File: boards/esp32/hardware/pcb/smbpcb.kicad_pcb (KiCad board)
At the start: 2 copper layers, 85.4 x 70.4 mm, 70 parts, among them IC1 MiCS-6814, J1 USB_B_Micro, J2 PMS7003, Q1 SUD08P06-155L, SW1 RESET, SW2 RESET, U1 MCP73831-2-OT, U2 SGM6603-5.0YN6G_TR, U3 ESP32-WROOM-32, U4 SSD1306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

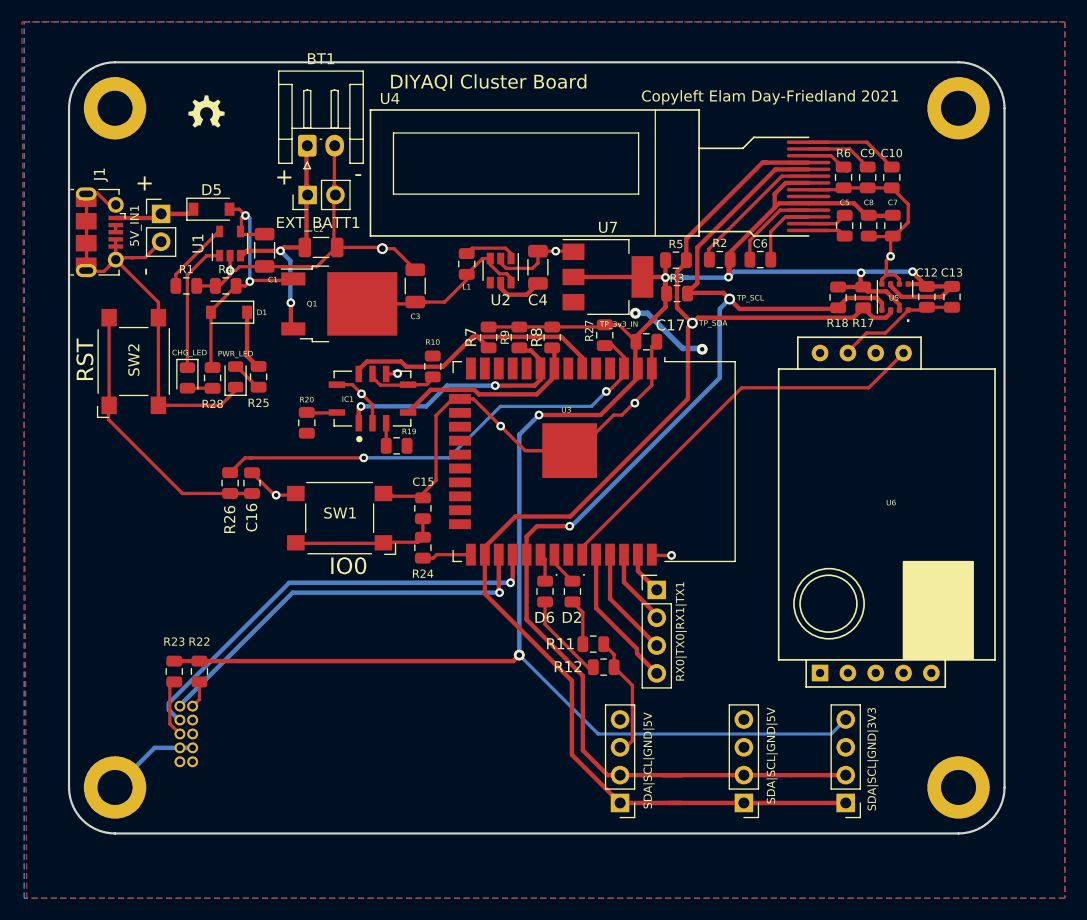
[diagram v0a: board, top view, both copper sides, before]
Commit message: went through DRC
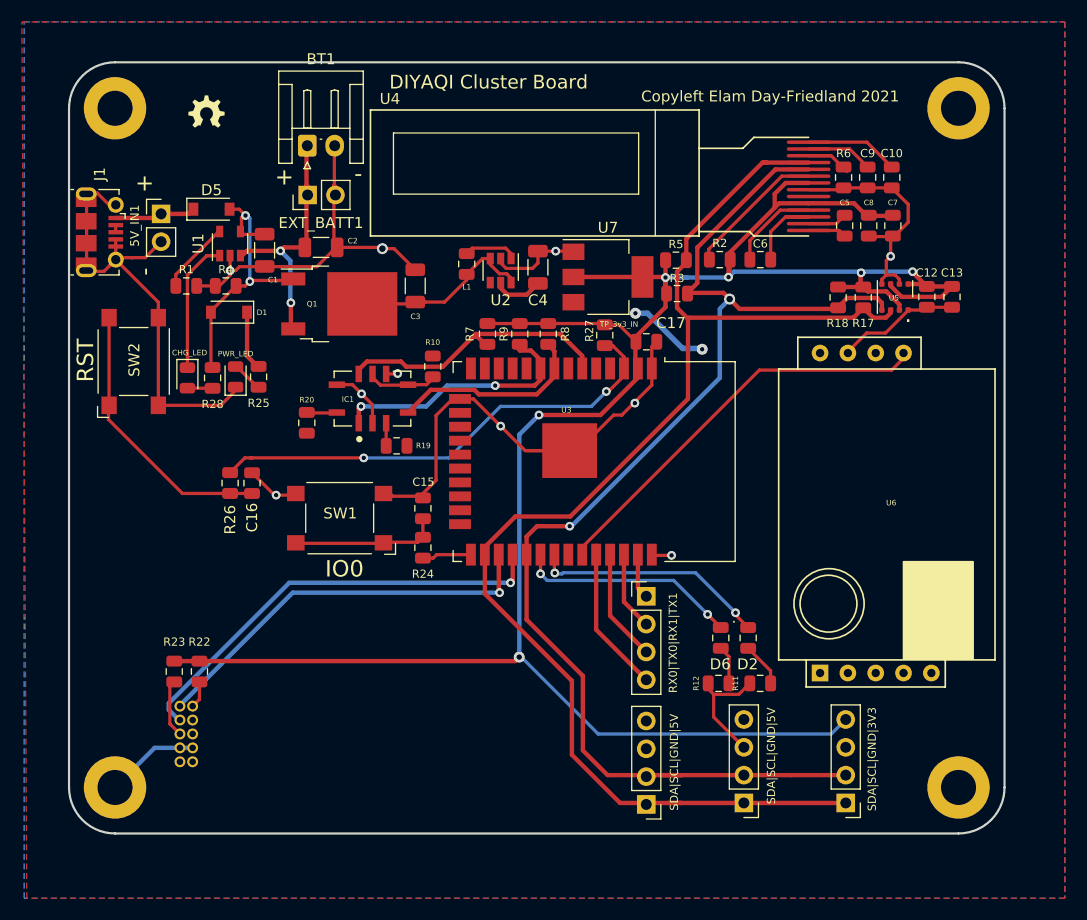
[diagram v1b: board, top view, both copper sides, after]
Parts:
- moved D2 16.6 mm to (113.5, 74.2)
- moved D6 16.6 mm to (111.0, 74.2)
- moved R11 15.7 mm to (114.7, 78.4), turned to 0 degrees
- moved R12 10.6 mm to (110.8, 78.4), turned to 0 degrees
- moved AUX_CONN2 2.39 mm to (104.2, 89.5)
- moved AUX_CONN1 1.12 mm to (104.2, 70.5)
- moved R8 0.48 mm to (95.3, 46.5)
- moved R7 0.33 mm to (89.8, 46.5)
- moved R9 0.32 mm to (92.7, 46.5)
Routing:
- net LED_BLUE: track 3.10 -> 22.4 mm, vias 0 -> 2
- net LED_GREEN: track 2.59 -> 20.2 mm, vias 0 -> 2
- net Net-(D6-Pad1): track 8.07 -> 3.51 mm
- net SDA: track 123.9 -> 123.8 mm, vias 1 -> 0
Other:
- board text removed: "TP_SCL"
- board text removed: "TP_SDA"

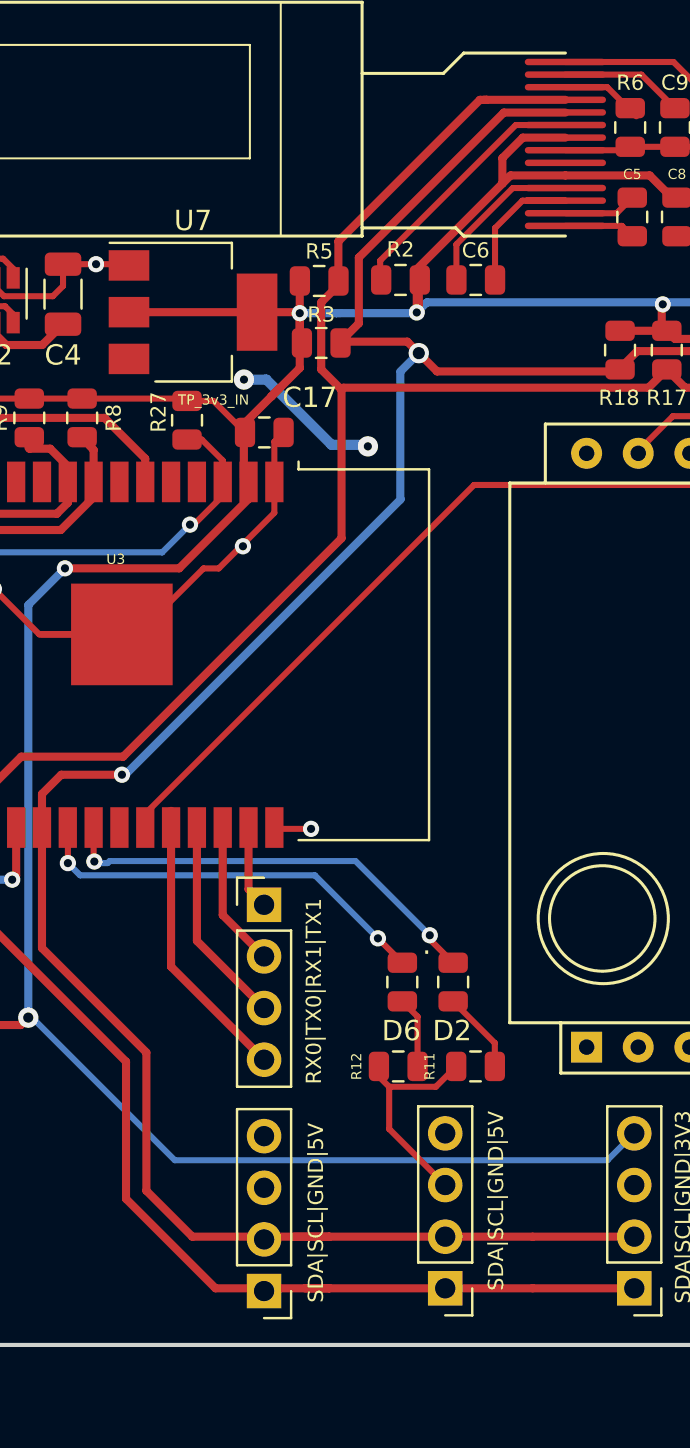
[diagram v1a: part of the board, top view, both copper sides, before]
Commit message: removed oled reset pullup it broke the oled
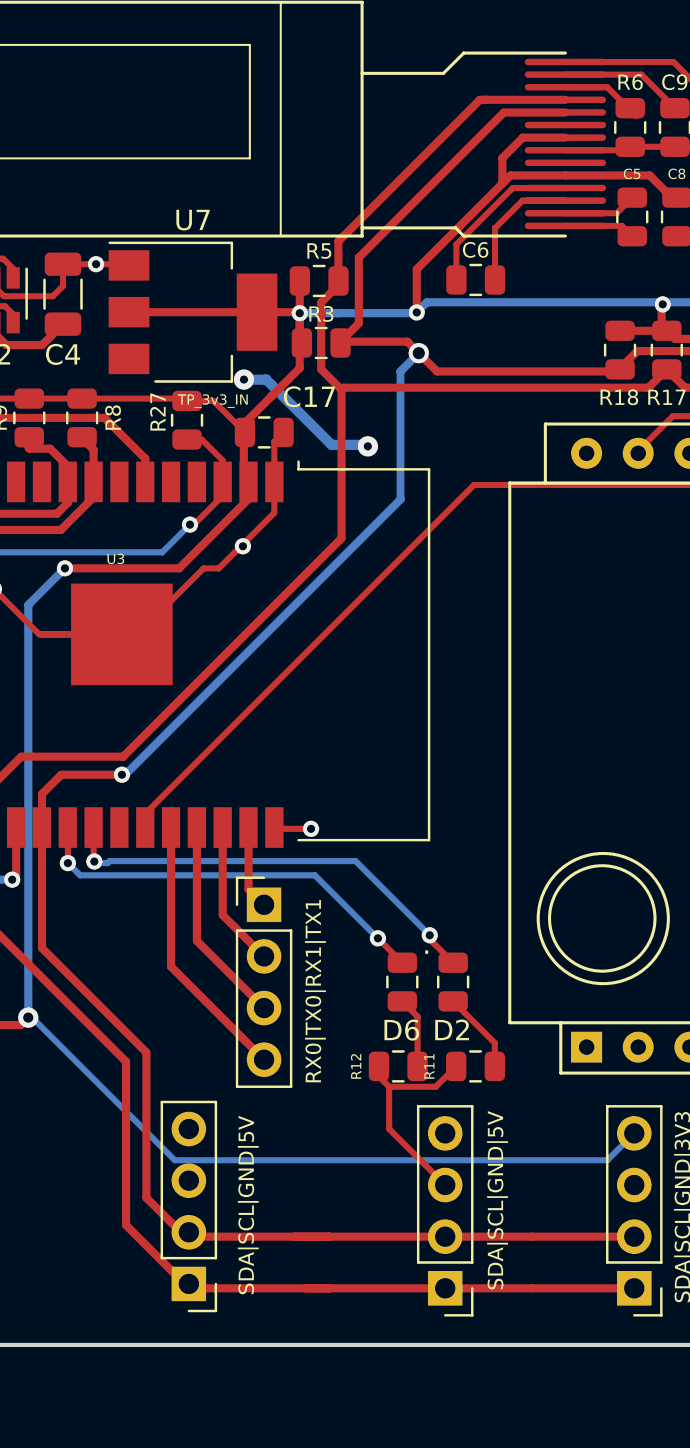
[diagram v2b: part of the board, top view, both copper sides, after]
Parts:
- removed R2: 10k, Capacitor_SMD:C_0805_2012Metric
- moved AUX_CONN2 3.72 mm to (100.5, 89.1)
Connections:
- U4 pad 9: Net-(R2-Pad2) -> +3V3
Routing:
- net Net-(R2-Pad2): track 13.0 -> 0.00 mm
- net +3V3: track 202.5 -> 201.2 mm
- net SDA: track 123.8 -> 124.6 mm

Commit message: more minor stuff
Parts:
- moved AUX_CONN2 3.71 mm to (104.2, 89.3)
- moved J2 1.77 mm to (78.6, 73.7)
- moved R22 1.21 mm to (62.2, 77.3)
- moved R23 1.21 mm to (60.0, 77.3)
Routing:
- net ESP_TX2: track 36.7 -> 38.8 mm
- net ESP_RX2: track 40.4 -> 42.5 mm
- net GND: track 200.5 -> 198.7 mm
- net Net-(J2-Pad10): track 2.47 -> 3.72 mm
- net Net-(J2-Pad5): track 5.30 -> 6.41 mm
